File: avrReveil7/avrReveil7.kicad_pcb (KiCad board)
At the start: 2 copper layers, 129.5 x 47.5 mm, 6 parts, among them J1 Conn_01x06, J2 Conn_01x06, J3 Conn_01x04, U1 TM1637

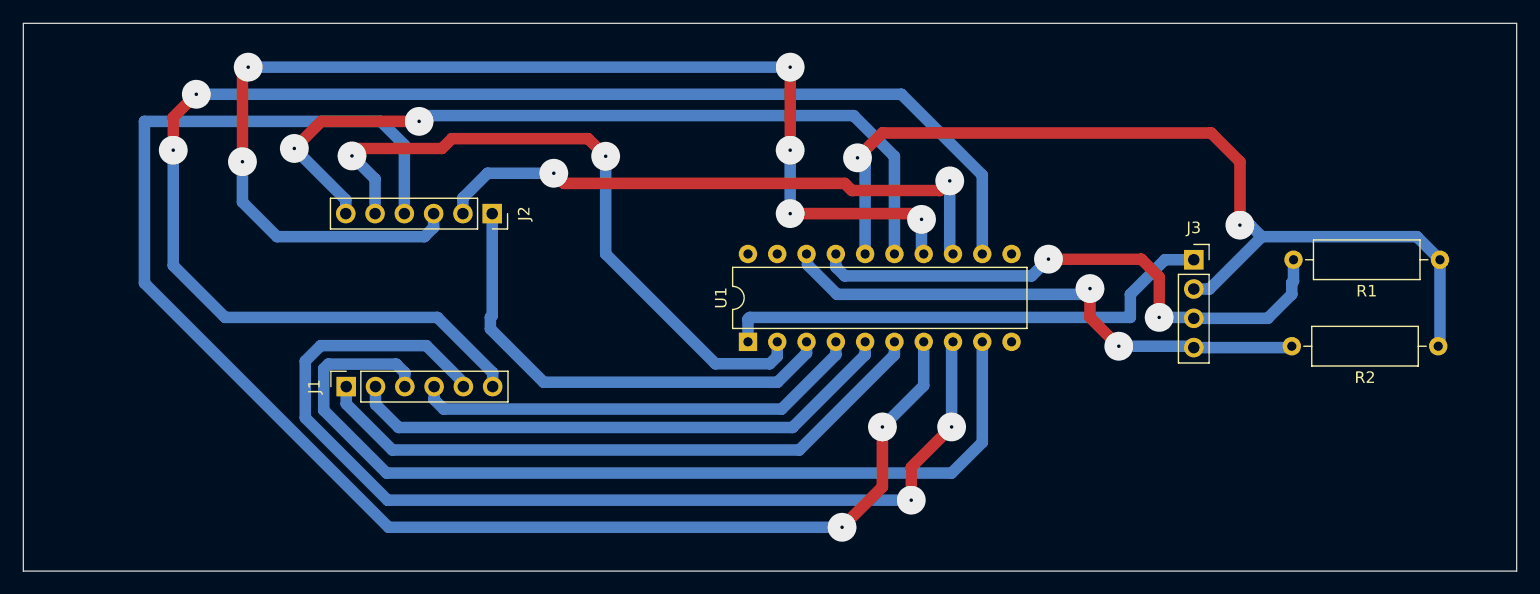
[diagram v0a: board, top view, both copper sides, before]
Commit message: board ready for home production
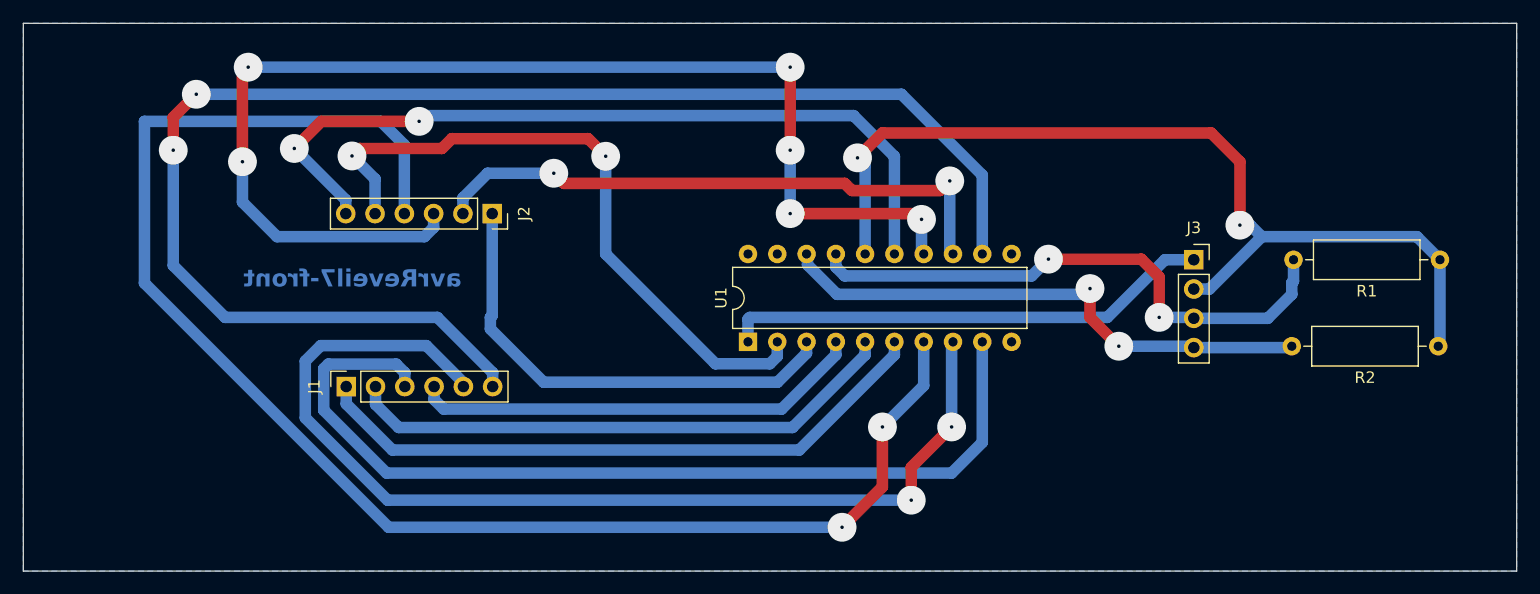
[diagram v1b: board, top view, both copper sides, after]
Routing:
- net GND: track 43.9 -> 42.8 mm
- added copper zone on B.Cu, net (none)
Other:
- board text added: "avrReveil7-front"
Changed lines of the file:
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@@
 		(allow_soldermask_bridges_in_footprints no)
 		(pcbplotparams
-			(layerselection 0x00010fc_ffffffff)
-			(plot_on_all_layers_selection 0x0000000_00000000)
+			(layerselection 0x0001000_fffffffe)
+			(plot_on_all_layers_selection 0x0001000_00000000)
 			(disableapertmacros no)
 			(usegerberextensions no)
@@
 			(outputformat 1)
 			(mirror no)
-			(drillshape 1)
+			(drillshape 0)
 			(scaleselection 1)
 			(outputdirectory "")
@@
 		(tags "Resistor Axial_DIN0309 series Axial Horizontal pin pitch 12.7mm 0.5W = 1/2W length 9mm diameter 3.2mm")
 		(property "Reference" "R1"
-			(at 6.35 -2.72 360)
+			(at 6.35 -2.72 0)
 			(layer "F.SilkS")
 			(effects
@@
 		)
 		(property "Value" "10k"
-			(at 6.35 2.72 360)
+			(at 6.35 2.72 0)
 			(layer "F.Fab")
 			(effects
@@
 		)
 		(fp_text user "${REFERENCE}"
-			(at 6.35 0 360)
+			(at 6.35 0 0)
 			(layer "F.Fab")
 			(effects
@@
 		)
 		(fp_text user "${REFERENCE}"
-			(at 0 6.35 360)
+			(at 0 6.35 0)
 			(layer "F.Fab")
 			(effects
@@
 		(tags "Resistor Axial_DIN0309 series Axial Horizontal pin pitch 12.7mm 0.5W = 1/2W length 9mm diameter 3.2mm")
 		(property "Reference" "R2"
-			(at 6.35 -2.72 360)
+			(at 6.35 -2.72 0)
 			(layer "F.SilkS")
 			(effects
@@
 		)
 		(property "Value" "10k"
-			(at 6.35 2.72 360)
+			(at 6.35 2.72 0)
 			(layer "F.Fab")
 			(effects
@@
 		)
 		(fp_text user "${REFERENCE}"
-			(at 6.35 0 360)
+			(at 6.35 0 0)
 			(layer "F.Fab")
 			(effects
@@
 		(tags "Through hole socket strip THT 1x04 2.54mm single row")
 		(property "Reference" "J3"
-			(at 0 -2.77 360)
+			(at 0 -2.77 0)
 			(layer "F.SilkS")
 			(effects
@@
 		)
 		(property "Value" "Conn_01x04"
-			(at 0 10.39 360)
+			(at 0 10.39 0)
 			(layer "F.Fab")
 			(effects
@@
 		(layer "Edge.Cuts")
 	)
+	(gr_text "avrReveil7-front"
+		(at 128 108.5 0)
+		(layer "B.Cu")
+		(effects
+			(font
+				(size 1.5 1.5)
+				(thickness 0.3)
+				(bold yes)
+			)
+			(justify left bottom mirror)
+		)
+	)
 	(gr_text "7 segment"
 		(at 120 109.5 0)
@@
 	)
 	(segment
-		(start 153 111)
-		(end 186 111)
+		(start 184 111)
+		(end 189 106)
 		(width 1)
 		(layer "B.Cu")
@@
 	)
 	(segment
-		(start 186 109)
-		(end 189 106)
+		(start 189 106)
+		(end 191.5 106)
 		(width 1)
 		(layer "B.Cu")
@@
 	)
 	(segment
-		(start 186 111)
-		(end 186 109)
+		(start 152.84 113.12)
+		(end 152.84 111.16)
 		(width 1)
 		(layer "B.Cu")
@@
 	)
 	(segment
-		(start 189 106)
-		(end 191.5 106)
-		(width 1)
-		(layer "B.Cu")
-		(net 14)
-	)
-	(segment
-		(start 152.84 113.12)
-		(end 152.84 111.16)
+		(start 153 111)
+		(end 184 111)
 		(width 1)
 		(layer "B.Cu")
@@
 			)
 		)
+	)
+	(zone
+		(net 0)
+		(net_name "")
+		(layer "B.Cu")
+		(hatch edge 0.5)
+		(connect_pads
+			(clearance 1)
+		)
+		(min_thickness 1)
+		(filled_areas_thickness no)
+		(fill yes
+			(thermal_gap 1)
+			(thermal_bridge_width 1)
+			(island_removal_mode 1)
+			(island_area_min 10)
+		)
+		(polygon
+			(pts
+				(xy 90 85.5) (xy 219.5 85.5) (xy 219.5 133) (xy 90 133)
+			)
+		)
